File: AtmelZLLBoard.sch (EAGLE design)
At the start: 8 parts

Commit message: Replaced resistors
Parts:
- R1, R2, R3: device resistor:R-EU_0207/7 -> resistor:R-EU_0204/5
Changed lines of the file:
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@@
 <part name="GND2" library="supply1" deviceset="GND" device=""/>
 <part name="U$2" library="osram_led" deviceset="LRTB_GFTG" device=""/>
-<part name="R1" library="resistor" deviceset="R-EU_" device="0207/7" value="5.6R"/>
-<part name="R2" library="resistor" deviceset="R-EU_" device="0207/7" value="5.6R"/>
-<part name="R3" library="resistor" deviceset="R-EU_" device="0207/7" value="68"/>
+<part name="R1" library="resistor" deviceset="R-EU_" device="0204/5" value="5.6R"/>
+<part name="R2" library="resistor" deviceset="R-EU_" device="0204/5" value="5.6R"/>
+<part name="R3" library="resistor" deviceset="R-EU_" device="0204/5" value="68"/>
 <part name="GND3" library="supply1" deviceset="GND" device=""/>
 <part name="JP1" library="pinhead" deviceset="PINHD-1X2" device=""/>

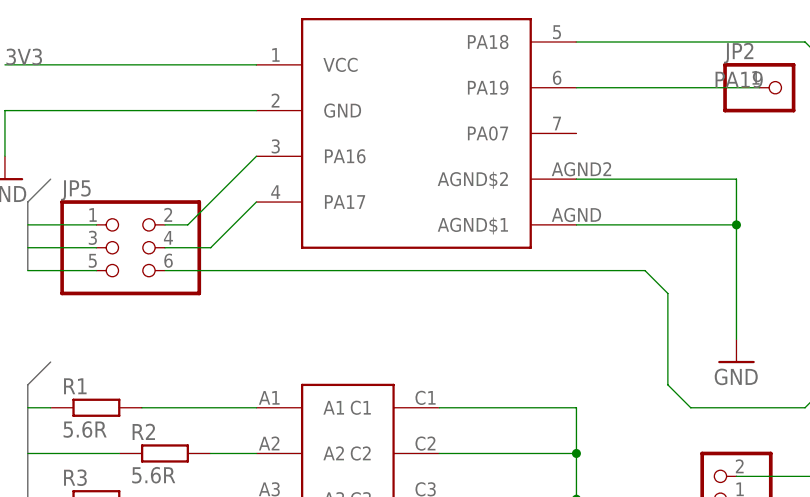
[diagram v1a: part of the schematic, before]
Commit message: Rewired stuff, added extra via's. Changed board dimensions.
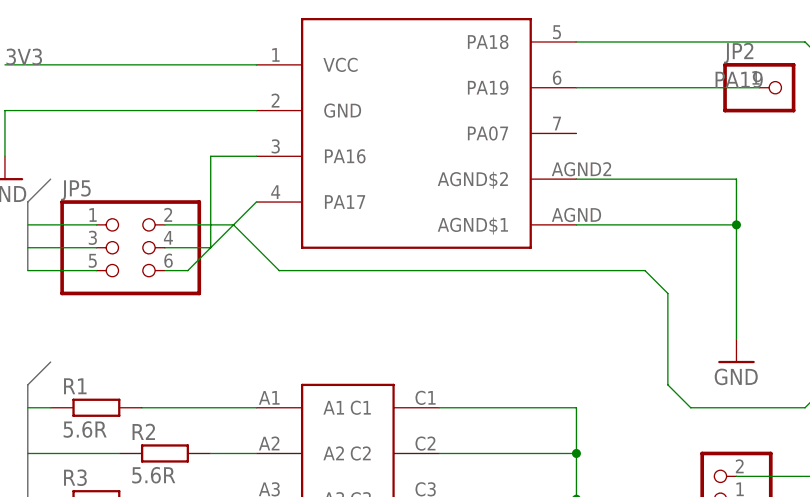
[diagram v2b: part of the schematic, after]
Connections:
- removed net N$1: JP5.2, U$1.PA16
- new net N$7: JP5.6, U$1.PA16
- net N$6: now also JP5.2; no longer JP5.6
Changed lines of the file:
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@@
 <?xml version="1.0" encoding="utf-8"?>
 <!DOCTYPE eagle SYSTEM "eagle.dtd">
-<eagle version="7.6.0">
+<eagle version="7.5.0">
 <drawing>
 <settings>
@@
 </segment>
 </net>
-<net name="N$1" class="0">
-<segment>
-<pinref part="U$1" gate="G$1" pin="PA16"/>
-<wire x1="38.1" y1="35.56" x2="30.48" y2="27.94" width="0.1524" layer="91"/>
-<pinref part="JP5" gate="A" pin="2"/>
-<wire x1="30.48" y1="27.94" x2="27.94" y2="27.94" width="0.1524" layer="91"/>
-</segment>
-</net>
-<net name="N$5" class="0">
-<segment>
-<pinref part="U$1" gate="G$1" pin="PA17"/>
-<wire x1="38.1" y1="30.48" x2="33.02" y2="25.4" width="0.1524" layer="91"/>
-<pinref part="JP5" gate="A" pin="4"/>
-<wire x1="33.02" y1="25.4" x2="27.94" y2="25.4" width="0.1524" layer="91"/>
-</segment>
-</net>
 <net name="N$6" class="0">
 <segment>
@@
 <wire x1="83.82" y1="10.16" x2="83.82" y2="20.32" width="0.1524" layer="91"/>
 <wire x1="83.82" y1="20.32" x2="81.28" y2="22.86" width="0.1524" layer="91"/>
-<pinref part="JP5" gate="A" pin="6"/>
-<wire x1="81.28" y1="22.86" x2="27.94" y2="22.86" width="0.1524" layer="91"/>
+<pinref part="JP5" gate="A" pin="2"/>
+<wire x1="27.94" y1="27.94" x2="35.56" y2="27.94" width="0.1524" layer="91"/>
+<wire x1="35.56" y1="27.94" x2="40.64" y2="22.86" width="0.1524" layer="91"/>
+<wire x1="40.64" y1="22.86" x2="81.28" y2="22.86" width="0.1524" layer="91"/>
 </segment>
 </net>
@@
 </segment>
 </net>
+<net name="N$5" class="0">
+<segment>
+<pinref part="JP5" gate="A" pin="4"/>
+<pinref part="U$1" gate="G$1" pin="PA17"/>
+<wire x1="27.94" y1="25.4" x2="33.02" y2="25.4" width="0.1524" layer="91"/>
+<wire x1="33.02" y1="25.4" x2="38.1" y2="30.48" width="0.1524" layer="91"/>
+</segment>
+</net>
+<net name="N$7" class="0">
+<segment>
+<pinref part="U$1" gate="G$1" pin="PA16"/>
+<wire x1="38.1" y1="35.56" x2="33.02" y2="35.56" width="0.1524" layer="91"/>
+<wire x1="33.02" y1="35.56" x2="33.02" y2="25.4" width="0.1524" layer="91"/>
+<wire x1="33.02" y1="25.4" x2="30.48" y2="22.86" width="0.1524" layer="91"/>
+<pinref part="JP5" gate="A" pin="6"/>
+<wire x1="30.48" y1="22.86" x2="27.94" y2="22.86" width="0.1524" layer="91"/>
+</segment>
+</net>

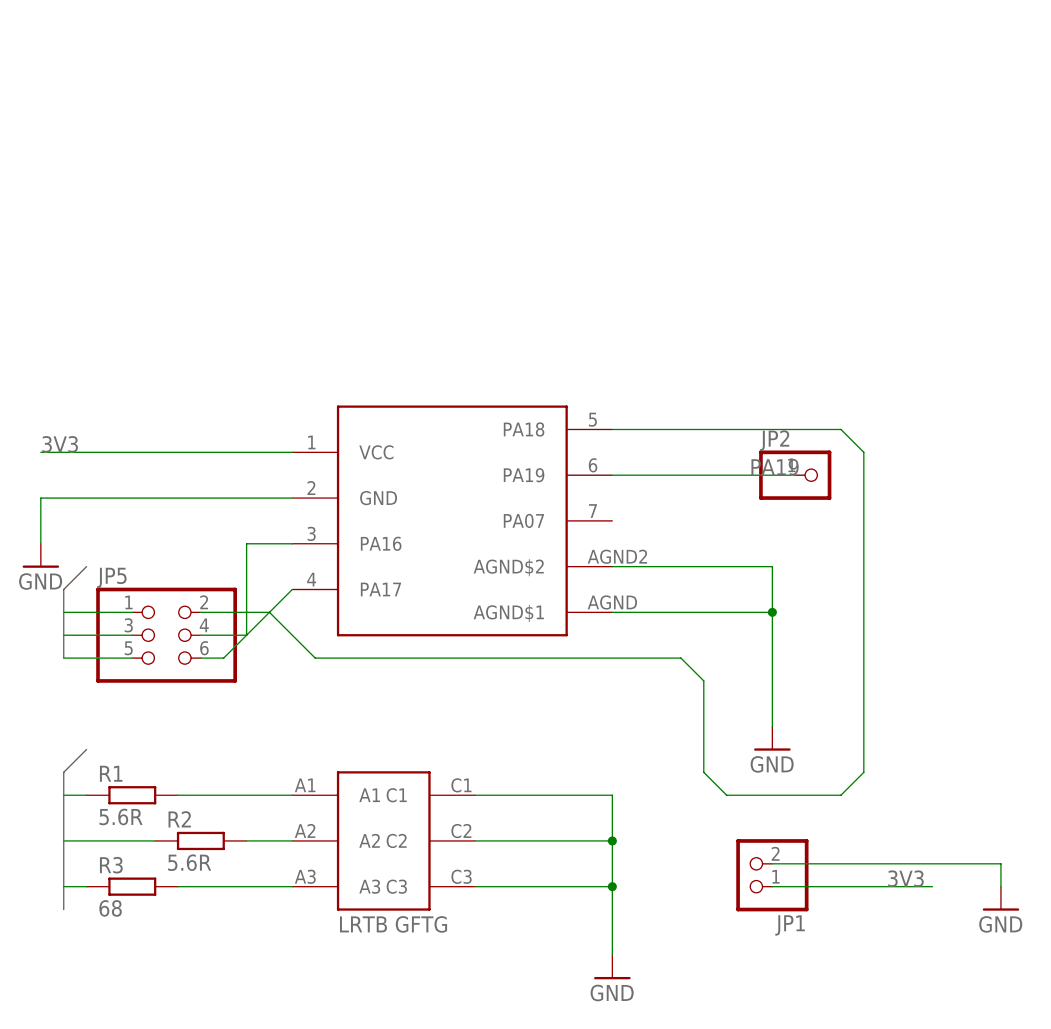
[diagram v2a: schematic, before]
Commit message: Replaced the regalar module with the module that contains the dev pads. Decreased the pad size, added oshpark rules for DRC. Added extra header onto the board that routes the programming pins.
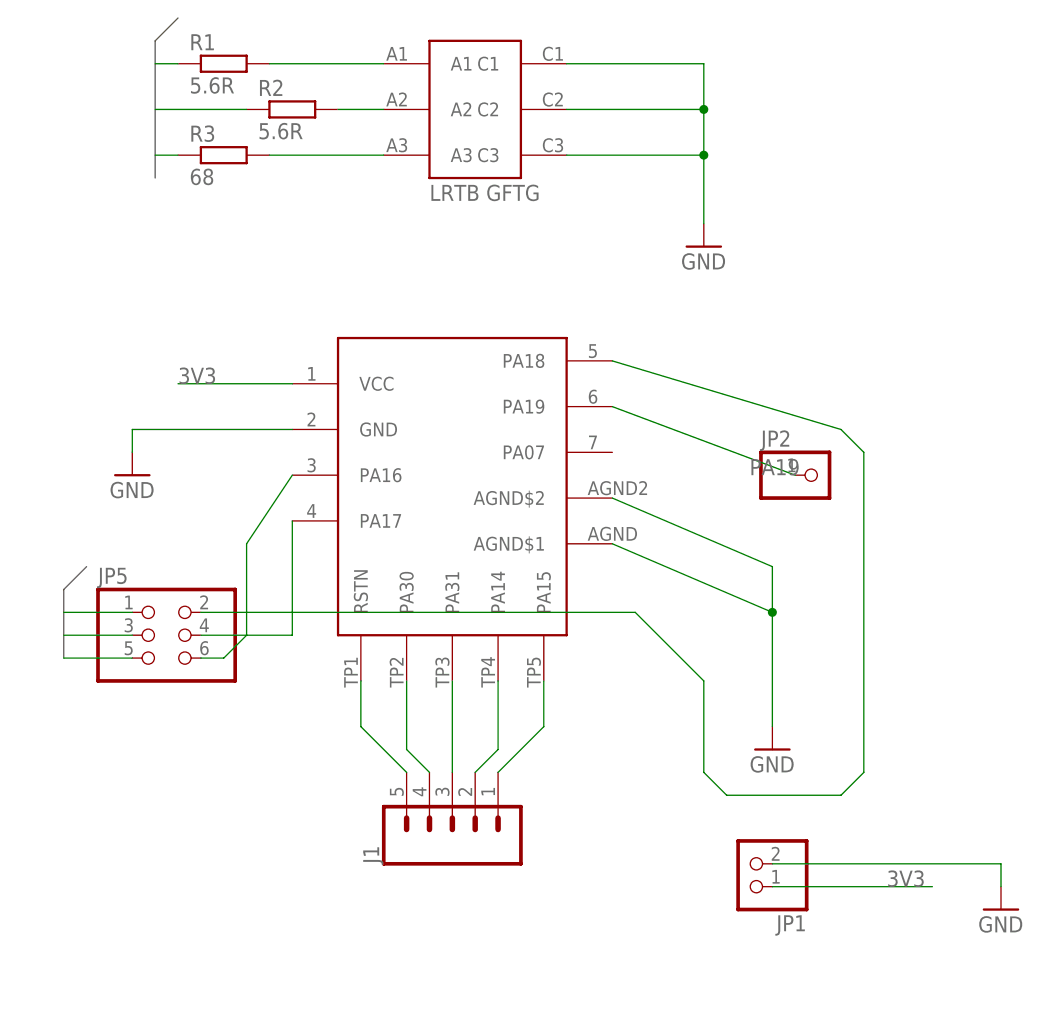
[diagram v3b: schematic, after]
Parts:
- added J1: (no value), SparkFun-Connectors:CONN_05LOCK
- U$1: value ATSAMR21B18-MZ210PA -> ATSAMR21B18-MZ210PA-DEV; device atmel-zll:ATSAMR21B18-MZ210PA -> atmel-zll:ATSAMR21B18-MZ210PA-DEV
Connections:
- new net N$1: J1.5, U$1.RSTN
- new net N$10: J1.2, U$1.PA14
- new net N$11: J1.1, U$1.PA15
- new net N$8: J1.4, U$1.PA30
- new net N$9: J1.3, U$1.PA31
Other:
- moved on the sheet: R1, R2, R3
